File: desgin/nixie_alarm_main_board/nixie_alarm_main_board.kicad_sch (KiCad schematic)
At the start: 11 parts, among them U1 ESP32-S3-WROOM-1

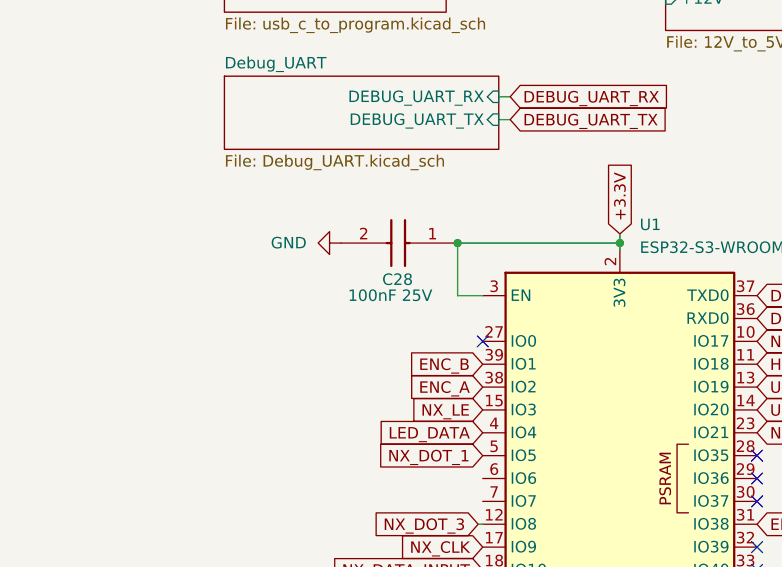
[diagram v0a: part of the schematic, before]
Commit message: added buttons
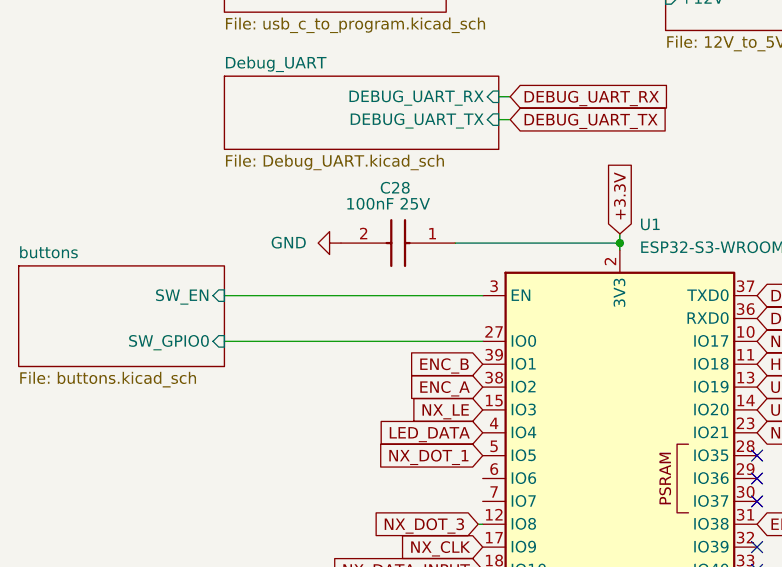
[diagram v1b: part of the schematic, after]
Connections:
- net +3.3V: no longer U1.3 (EN)
- net buttons/SW_GPIO0: now reaches U1.27 (IO0)
- new net buttons/SW_EN: U1.3 (EN)
- no-connect marks 9 -> 8
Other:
- added sheet buttons (buttons.kicad_sch)
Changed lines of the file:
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@@
-		(color 0 0 0 0)
-	)
-	(junction
-		(at 109.474 81.28)
-		(diameter 0)
 		(color 0 0 0 0)
 	)
@@
 	)
 	(no_connect
-		(at 112.268 92.202)
-	)
-	(no_connect
 		(at 142.748 122.682)
 	)
@@
 	(wire
 		(pts
-			(xy 109.474 81.28) (xy 127.508 81.28)
+			(xy 109.22 81.28) (xy 127.508 81.28)
 		)
 		(stroke
@@
 	(wire
 		(pts
-			(xy 109.474 87.122) (xy 109.474 81.28)
-		)
-		(stroke
-			(width 0)
-			(type default)
-		)
-	)
-	(wire
-		(pts
 			(xy 190.754 85.09) (xy 191.77 85.09)
 		)
@@
 	(wire
 		(pts
+			(xy 112.268 92.202) (xy 83.566 92.202)
+		)
+		(stroke
+			(width 0)
+			(type default)
+		)
+	)
+	(wire
+		(pts
 			(xy 153.67 54.61) (xy 165.862 54.61)
 		)
@@
 	(wire
 		(pts
+			(xy 83.566 87.122) (xy 112.268 87.122)
+		)
+		(stroke
+			(width 0)
+			(type default)
+		)
+	)
+	(wire
+		(pts
 			(xy 123.19 153.67) (xy 128.27 153.67)
 		)
@@
 	(wire
 		(pts
-			(xy 109.22 81.28) (xy 109.474 81.28)
-		)
-		(stroke
-			(width 0)
-			(type default)
-		)
-	)
-	(wire
-		(pts
 			(xy 190.754 77.47) (xy 191.77 77.47)
 		)
@@
 		(pts
 			(xy 169.926 33.528) (xy 179.832 33.528)
-		)
-		(stroke
-			(width 0)
-			(type default)
-		)
-	)
-	(wire
-		(pts
-			(xy 112.268 87.122) (xy 109.474 87.122)
 		)
 		(stroke
@@
 		(dnp no)
 		(property "Reference" "C28"
-			(at 101.092 85.344 0)
+			(at 100.838 75.184 0)
 			(effects
 				(font
@@
 		)
 		(property "Value" "100nF 25V"
-			(at 97.282 87.122 0)
+			(at 97.028 76.962 0)
 			(effects
 				(font
@@
 				)
 			)
+		)
+	)
+	(sheet
+		(at 60.706 83.82)
+		(size 22.86 11.176)
+		(fields_autoplaced yes)
+		(stroke
+			(width 0.1524)
+			(type solid)
+		)
+		(fill
+			(color 0 0 0 0.0000)
+		)
+		(property "Sheetname" "buttons"
+			(at 60.706 83.1084 0)
+			(effects
+				(font
+					(size 1.27 1.27)
+				)
+				(justify left bottom)
+			)
+		)
+		(property "Sheetfile" "buttons.kicad_sch"
+			(at 60.706 95.5806 0)
+			(effects
+				(font
+					(size 1.27 1.27)
+				)
+				(justify left top)
+			)
+		)
+		(pin "SW_EN" input
+			(at 83.566 87.122 0)
+			(effects
+				(font
+					(size 1.27 1.27)
+				)
+				(justify right)
+			)
+		)
+		(pin "SW_GPIO0" input
+			(at 83.566 92.202 0)
+			(effects
+				(font
+					(size 1.27 1.27)
+				)
+				(justify right)
+			)
+		)
+		(instances
+			(project "nixie_alarm_main_board"
+				(path "/a0d555d7-39a0-4a98-b831-70d97d0aa5a1"
+					(page "12")
+				)
+			)
